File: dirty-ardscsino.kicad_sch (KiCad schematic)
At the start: 16 parts, among them J1 SCSI, J2 171825-4 (Ext. Power), J3 DM3AT-SF-PEJM5, U1 STM32 Bluepill, U2 microSD-Breakout

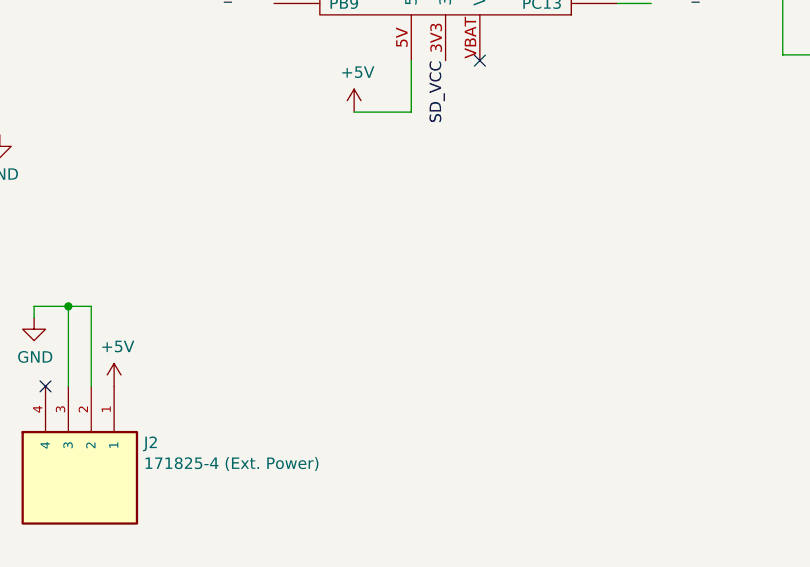
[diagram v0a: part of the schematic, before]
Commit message: Fix broken MISO/MOSI traces
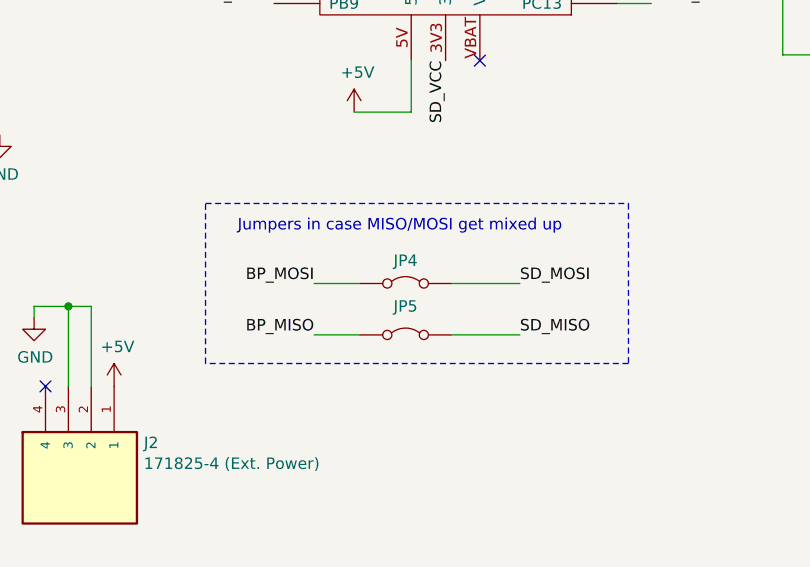
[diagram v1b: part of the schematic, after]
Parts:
- added JP4, JP5: Jumper_2_Bridged, Jumper:SolderJumper-2_P1.3mm_Bridged_RoundedPad1.0x1.5mm, symbol Jumper:Jumper_2_Bridged
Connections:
- net BP_MISO: now also JP5.1 (A)
- net BP_MOSI: now also JP4.1 (A)
- net SD_MISO: now also JP5.2 (B)
- net SD_MOSI: now also JP4.2 (B)
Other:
- note added: "Jumpers in case MISO/MOSI get mixed up"

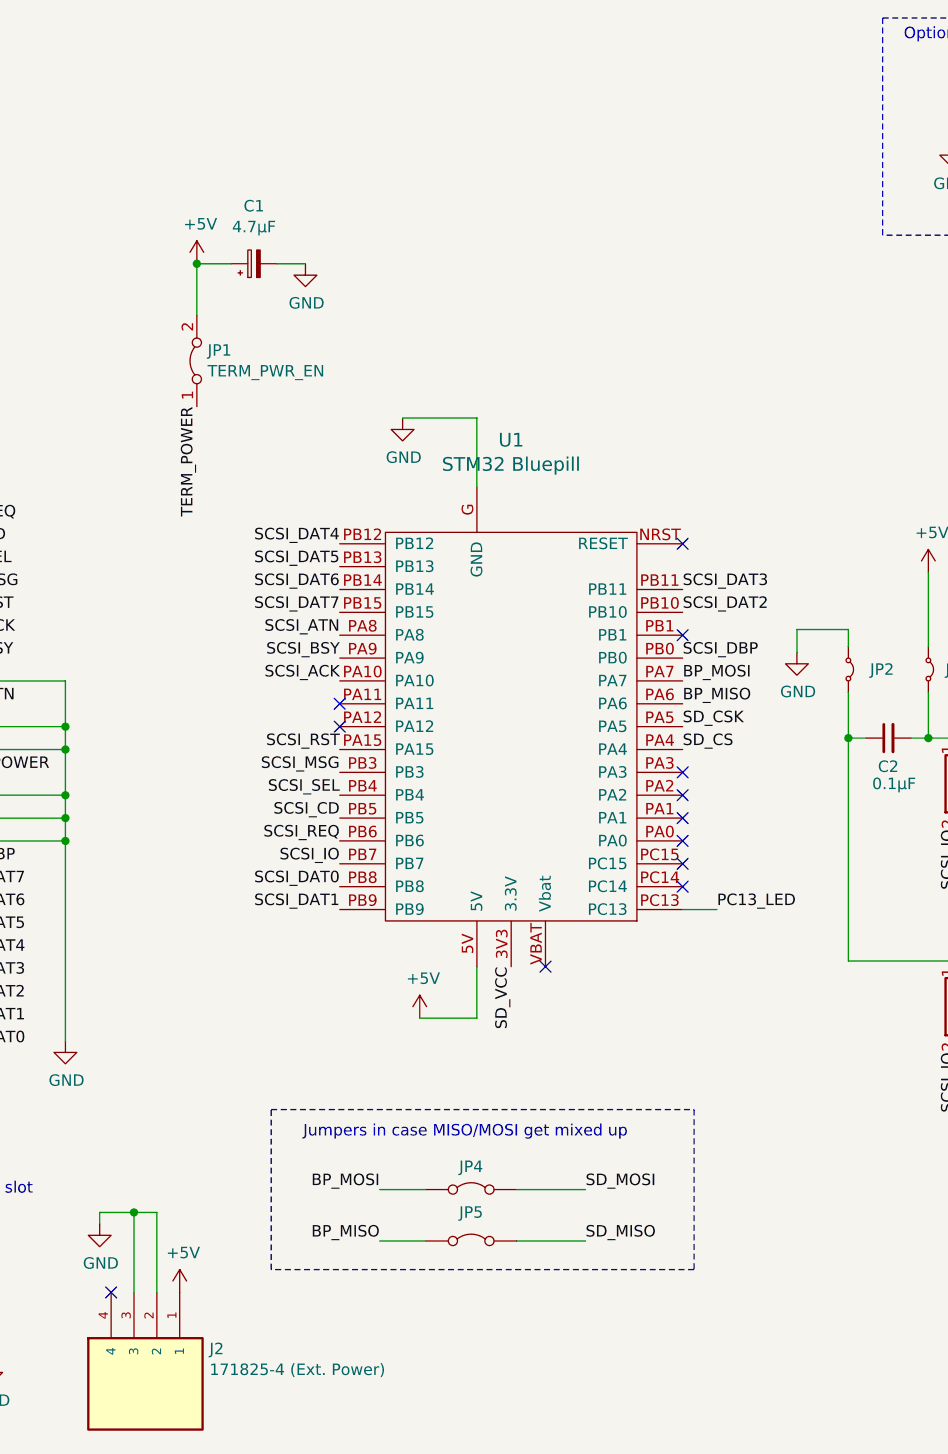
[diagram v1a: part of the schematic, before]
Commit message: add zener diodes
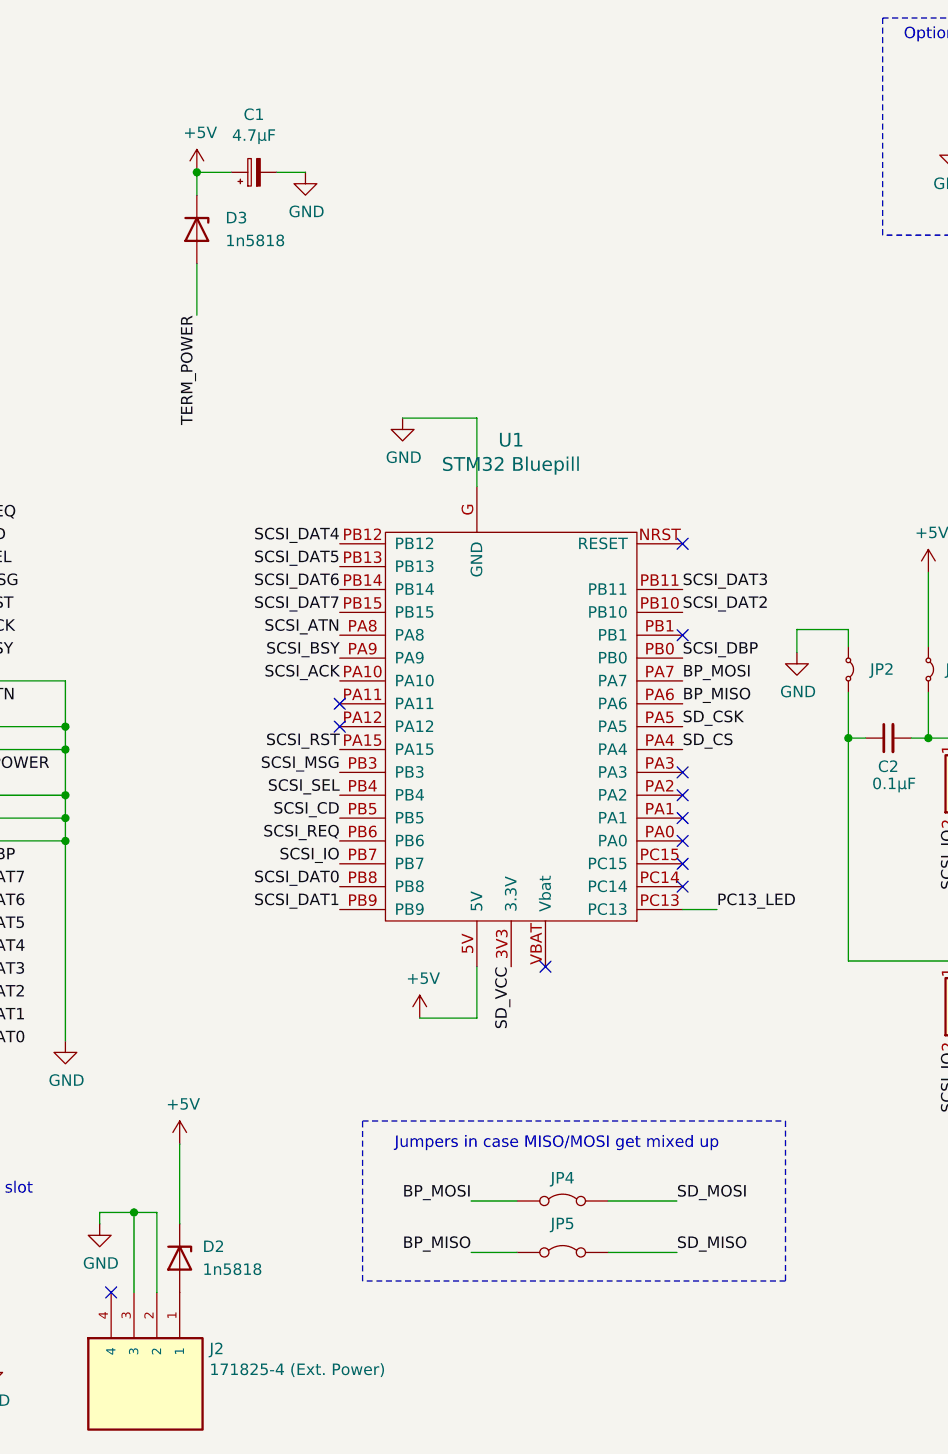
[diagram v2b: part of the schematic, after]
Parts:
- removed JP1: TERM_PWR_EN, Connector_PinHeader_2.54mm:PinHeader_1x02_P2.54mm_Vertical, symbol Jumper:Jumper_2_Bridged
- added D2, D3: 1n5818, Diode_THT:D_DO-41_SOD81_P7.62mm_Horizontal, symbol Device:D_Zener
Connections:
- net +5V: now also D2.1 (K), D3.1 (K); no longer J2.1
- net TERM_POWER: now also D3.2 (A)
- new net: D2.2 (A), J2.1
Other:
- moved on the sheet: C1, JP4, JP5
